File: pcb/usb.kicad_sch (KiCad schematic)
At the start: 11 parts

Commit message: Upgrade kicad version to 10, add krita capacitor image
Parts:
- D2, D4, D5, H4, Q1, USB1: value ~ -> (none)

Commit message: Add JLC carts and BOM
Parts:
- C8: Manufacturer Part (none) -> CL10B105KA8NNNC; Supplier (none) -> LCSC; Supplier Part C15849 -> C29936; Supplier Part URL (none) -> https://www.lcsc.com/product-detail/C29936.html
- D2: Supplier Part URL (none) -> https://www.lcsc.com/product-detail/C85098.html
- D4, D5: Manufacturer Part PTVSUC3D5VB -> PESD5V0U1BA-N; Supplier Part C918847 -> C406223; Supplier Part URL (none) -> https://www.lcsc.com/product-detail/C406223.html
- H4: now left out of the parts list
- Q1: Supplier Part URL (none) -> https://www.lcsc.com/product-detail/C5125736.html
- R1, R2: Manufacturer Part (none) -> FRC0603F5101TS; Supplier (none) -> LCSC; Supplier Part URL (none) -> https://www.lcsc.com/product-detail/C2907044.html
- R8: Manufacturer Part (none) -> RC0603FR-071KL; Supplier (none) -> LCSC; Supplier Part URL (none) -> https://www.lcsc.com/product-detail/C22548.html
- R9: Manufacturer Part (none) -> RC0603FR-07200KL; Supplier (none) -> LCSC; Supplier Part URL (none) -> https://www.lcsc.com/product-detail/C105574.html
- USB1: Supplier Part URL (none) -> https://www.lcsc.com/product-detail/C2765186.html

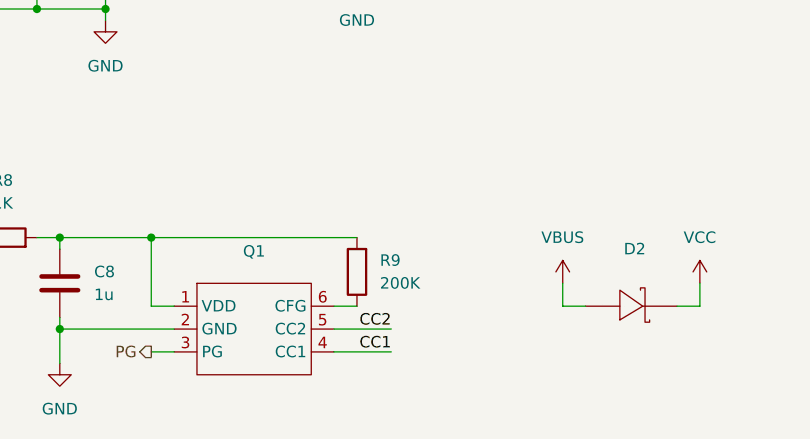
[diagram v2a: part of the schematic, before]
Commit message: Change input voltage range
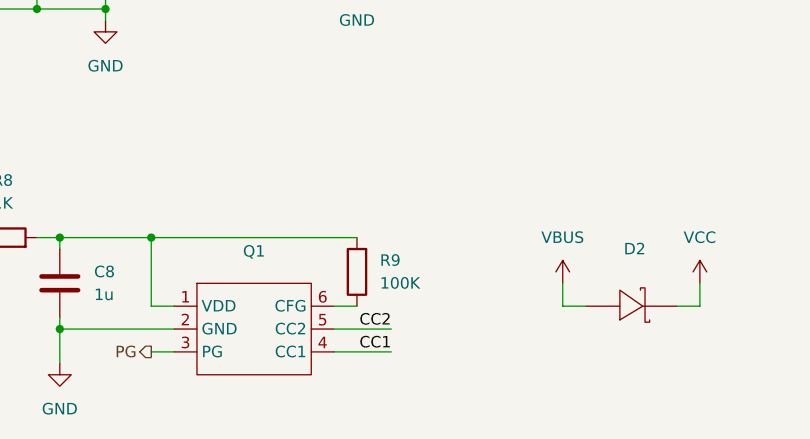
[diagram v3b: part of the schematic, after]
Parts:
- R9: value 200K -> 100K; Manufacturer Part RC0603FR-07200KL -> FRC0603F1003TS; Supplier Part C105574 -> C2906980; Supplier Part URL https://www.lcsc.com/product-detail/C105574.html -> https://www.lcsc.com/product-detail/C2906980.html
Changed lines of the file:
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@@
 			)
 		)
-		(property "Value" "200K"
+		(property "Value" "100K"
 			(at 95.25 95.2499 0)
 			(show_name no)
@@
 			)
 		)
-		(property "Supplier Part" "C105574"
+		(property "Supplier Part" "C2906980"
 			(at 92.71 93.98 0)
 			(hide yes)
@@
 			)
 		)
-		(property "Manufacturer Part" "RC0603FR-07200KL"
+		(property "Manufacturer Part" "FRC0603F1003TS"
 			(at 92.71 93.98 0)
 			(hide yes)
@@
 			)
 		)
-		(property "Supplier Part URL" "https://www.lcsc.com/product-detail/C105574.html"
+		(property "Supplier Part URL" "https://www.lcsc.com/product-detail/C2906980.html"
 			(at 92.71 93.98 0)
 			(hide yes)
